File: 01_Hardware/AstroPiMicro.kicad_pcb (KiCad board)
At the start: 2 copper layers, 65 x 50.2 mm, 46 parts, among them J1 RPi Connector, J2 USB_C_Receptacle_USB2.0, J3 Battery, J4 I2C_IMU, J5 DEBUG, J6 TFT_LCD, SW1 SW_SPDT, U1 LM809, U2 STM32G431KBTx, U3 MCP73831-2-OT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

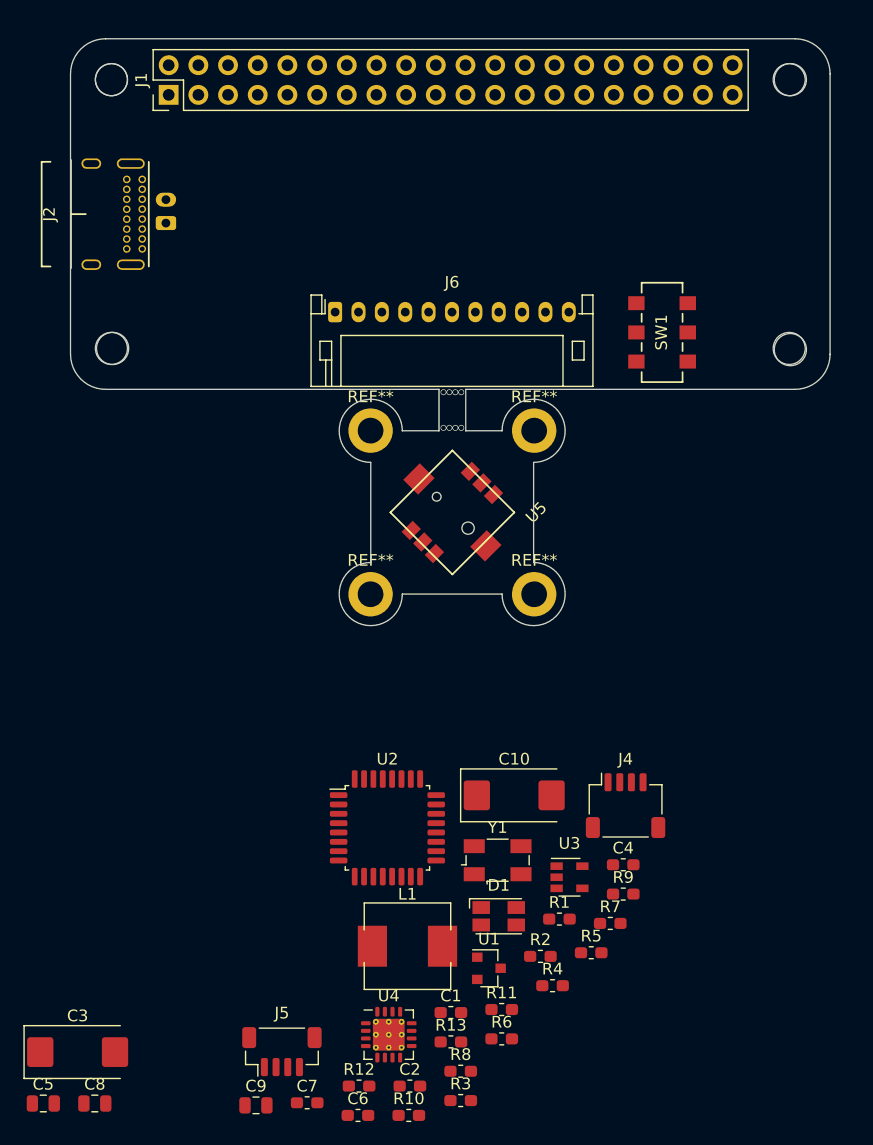
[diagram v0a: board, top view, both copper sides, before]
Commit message: Finished board outline
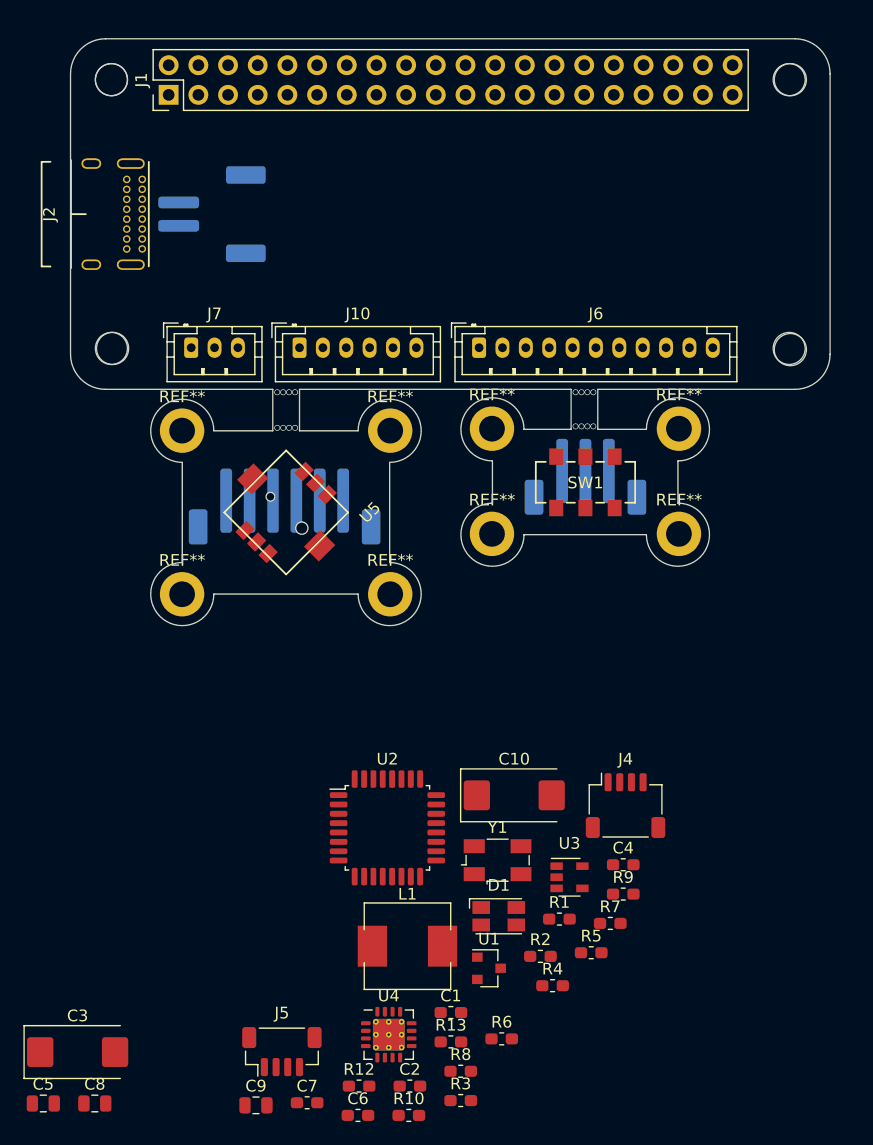
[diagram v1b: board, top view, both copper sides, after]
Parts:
- removed R11: 1k, Resistor_SMD:R_0603_1608Metric_Pad1.05x0.95mm_HandSolder
- added J10: CON_JOY_A, Connector_JST:JST_PH_B6B-PH-K_1x06_P2.00mm_Vertical, F.Cu at (69.6, 75.4)
- added J7: CON_SW_A, Connector_JST:JST_PH_B3B-PH-K_1x03_P2.00mm_Vertical, F.Cu at (60.3, 75.4)
- added J8: CON_SW_B, Connector_JST:JST_PH_B3B-PH-SM4-TB_1x03-1MP_P2.00mm_Vertical, B.Cu at (94.1, 86.5)
- added J9: CON_JOY_B, Connector_JST:JST_PH_B6B-PH-SM4-TB_1x06-1MP_P2.00mm_Vertical, B.Cu at (68.3, 89.0)
- added REF**: MountingHole_2.2mm_M2_ISO14580_Pad, MountingHole:MountingHole_2.2mm_M2_ISO14580_Pad, F.Cu at (86.1, 82.4)
- added REF**: MountingHole_2.2mm_M2_ISO14580_Pad, MountingHole:MountingHole_2.2mm_M2_ISO14580_Pad, F.Cu at (86.1, 91.4)
- added REF**: MountingHole_2.2mm_M2_ISO14580_Pad, MountingHole:MountingHole_2.2mm_M2_ISO14580_Pad, F.Cu at (102.1, 91.4)
- added REF**: MountingHole_2.2mm_M2_ISO14580_Pad, MountingHole:MountingHole_2.2mm_M2_ISO14580_Pad, F.Cu at (102.1, 82.4)
- J3: footprint Connector_JST:JST_PH_S2B-PH-K_1x02_P2.00mm_Horizontal -> Connector_JST:JST_PH_S2B-PH-SM4-TB_1x02-1MP_P2.00mm_Horizontal
- J6: footprint Connector_JST:JST_PH_S11B-PH-K_1x11_P2.00mm_Horizontal -> Connector_JST:JST_PH_B11B-PH-K_1x11_P2.00mm_Vertical
- moved SW1 18.8 mm to (91.6, 89.2), turned to 90 degrees
- moved REF** 16.1 mm to (59.5, 82.5)
- moved REF** 16.1 mm to (59.5, 96.5)
- moved U5 14.2 mm to (68.5, 89.5)
- moved J6 12.7 mm to (85.0, 75.4)
- moved REF** 12.3 mm to (77.4, 82.5)
- moved REF** 12.3 mm to (77.4, 96.5)
- moved J3 4.01 mm to (62.1, 64.0), turned to 270 degrees
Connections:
- J1 pad 11: Net-(J1-Pad11) -> /GPIO17
- J1 pad 13: Net-(J1-Pad13) -> /GPIO27
- J1 pad 15: Net-(J1-Pad15) -> /GPIO22
- J1 pad 16: Net-(J1-Pad16) -> /GPIO23
- J1 pad 7: Net-(J1-Pad7) -> /GPIO4
- SW1 pad 1: +BATT -> /SW_1
- SW1 pad 2: /ON\~OFF -> /SW_2
- SW1 pad 3: GND -> /SW_3
- U5 pad 1: /GPIO17 -> /JOY_A
- U5 pad 2: /GPIO4 -> /JOY_PUSH
- U5 pad 3: /GPIO22 -> /JOY_C
- U5 pad 4: /GPIO27 -> /JOY_B
- U5 pad 5: GND -> /JOY_GND
- U5 pad 6: /GPIO23 -> /JOY_D
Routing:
- net (no net): vias 8 -> 16
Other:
- outline, holes or cut-outs redrawn

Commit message: Routing finished.
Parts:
- removed C3: 100uF, Capacitor_Tantalum_SMD:CP_EIA-7343-31_Kemet-D_Pad2.25x2.55mm_HandSolder
- J4: moved to B.Cu
- moved C6 84.5 mm to (92.2, 58.5), turned to 180 degrees
- moved R8 82.4 mm to (66.5, 56.7)
- moved C7 81.5 mm to (89.1, 60.8), turned to 90 degrees
- moved C2 80.7 mm to (104.9, 62.2)
- moved C5 80.0 mm to (58.0, 60.8), turned to 90 degrees
- moved C9 78.4 mm to (71.6, 62.0), turned to 90 degrees
- moved R12 76.7 mm to (81.8, 62.3)
- moved R6 75.4 mm to (66.5, 62.0)
- moved R4 74.2 mm to (58.8, 63.3), turned to 180 degrees
- moved U1 73.3 mm to (104.9, 57.7)
- moved C8 72.6 mm to (71.1, 70.0), turned to 180 degrees
- moved R5 71.8 mm to (58.8, 65.0), turned to 180 degrees
- moved R7 71.1 mm to (63.0, 61.9)
- moved R13 70.9 mm to (81.8, 63.9), turned to 180 degrees
- moved J5 70.3 mm to (86.7, 67.9), turned to 270 degrees
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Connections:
- J1 pad 12: Net-(J1-Pad12) -> /~LOW_BAT
- J1 pad 37: /~LOW_BAT -> Net-(J1-Pad37)
- U4 pad 10: GND -> +BATT
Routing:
- net GND: track 0.00 -> 70.8 mm, vias 0 -> 23
- net +3V3: track 0.00 -> 61.6 mm, vias 0 -> 6
- net /IMU_SCL: track 0.00 -> 53.7 mm, vias 0 -> 5
- net /IMU_SDA: track 0.00 -> 51.0 mm, vias 0 -> 3
- net +BATT: track 0.00 -> 49.8 mm, vias 0 -> 2
- net +5V: track 0.00 -> 43.2 mm, vias 0 -> 1
- net /PI_UART_RX: track 0.00 -> 42.2 mm, vias 0 -> 2
- net /GPIO4: track 0.00 -> 41.3 mm, vias 0 -> 4
- net /PI_UART_TX: track 0.00 -> 39.6 mm, vias 0 -> 2
- net /LCD_BL: track 0.00 -> 34.9 mm, vias 0 -> 1
- net /GPIO22: track 0.00 -> 32.6 mm, vias 0 -> 1
- net /LCD_TDC: track 0.00 -> 31.0 mm, vias 0 -> 2
- net /GPIO23: track 0.00 -> 30.3 mm, vias 0 -> 4
- net /LCD_~TCS: track 0.00 -> 29.6 mm, vias 0 -> 4
- net /GPIO17: track 0.00 -> 28.7 mm, vias 0 -> 2
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- added copper zone on F.Cu, net +3V3
- added copper zone on F.Cu, net +5V
- added copper zone on B.Cu, net GND
- added copper zone on F.Cu, net GND
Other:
- rule trace_min: 0.2 -> 0.15
- rule via_min_drill: 0.3 -> 0.2
- rule via_min_size: 0.4 -> 0.45
- board text added: "<NP"
